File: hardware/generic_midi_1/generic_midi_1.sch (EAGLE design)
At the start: 26 parts, among them IC1 MEGA168/328, IC2 RFM12

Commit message: test
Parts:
- removed JP10: PD6, pinhead:PINHD-1X1
- removed JP11: PD4, pinhead:PINHD-1X1
- removed JP12: PD3, pinhead:PINHD-1X1
- removed JP13: PB7, pinhead:PINHD-1X1
- removed JP14: PD0, pinhead:PINHD-1X1
- removed JP9: PD5, pinhead:PINHD-1X1
- JP6: value PB1 -> (none); device pinhead:PINHD-1X1 -> pinhead:PINHD-1X8
- JP7: value PB2 -> (none); device pinhead:PINHD-1X1 -> pinhead:PINHD-1X2
- JP8: value PD1 -> (none)
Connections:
- removed net N$16: IC1.PD6(AIN0/OC0A/PCINT22), JP10.1
- removed net N$17: IC1.PB1(OC1A/PCINT1), JP6.1
- removed net N$19: IC1.PB2(SS/OC1B/PCINT2), JP7.1
- removed net N$20: IC1.PD1(TXD/PCINT17), JP8.1
- removed net N$22: IC1.PD4(T0/XCK/PCINT20), JP11.1
- removed net N$23: IC1.PD3(INT1/OC2B/PCINT19), JP12.1
- removed net N$25: IC1.PB7(XTAL2/TOSC2/PCINT7), JP13.1
- removed net N$26: IC1.PD0(RXD/PCINT16), JP14.1
- new net IO0: IC1.PD1(TXD/PCINT17), JP6.1
- new net IO1: IC1.PD0(RXD/PCINT16), JP6.2
- new net IO2: IC1.PD3(INT1/OC2B/PCINT19), JP6.3
- new net IO3: IC1.PD4(T0/XCK/PCINT20), JP6.4
- new net IO4: IC1.PD5(T1/OC0B/PCINT21), JP6.5
- new net IO5: IC1.PD6(AIN0/OC0A/PCINT22), JP6.6
- new net IO6: IC1.PB1(OC1A/PCINT1), JP6.7
- new net IO7: IC1.PB2(SS/OC1B/PCINT2), JP6.8
- net N$14: now also IC1.PB7(XTAL2/TOSC2/PCINT7), JP7.1, JP7.2; no longer IC1.PD5(T1/OC0B/PCINT21), JP9.1
- net N$24: now also JP8.1
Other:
- moved on the sheet: JP8, R2, R3

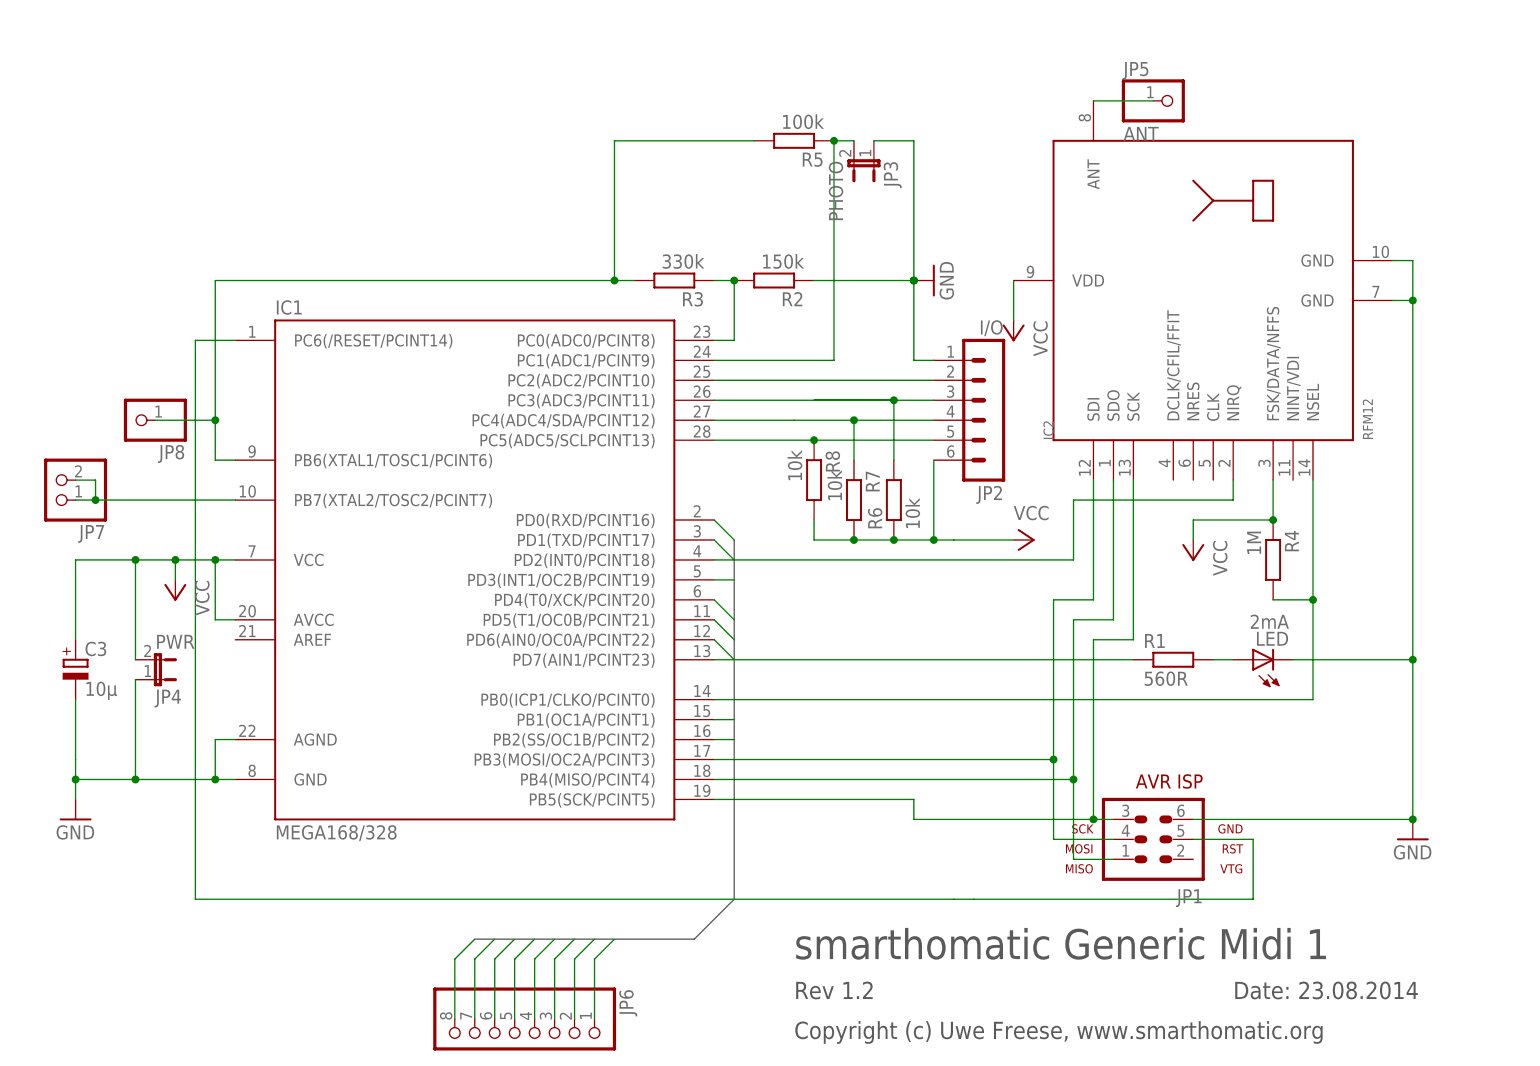
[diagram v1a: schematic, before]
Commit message: fix transistor
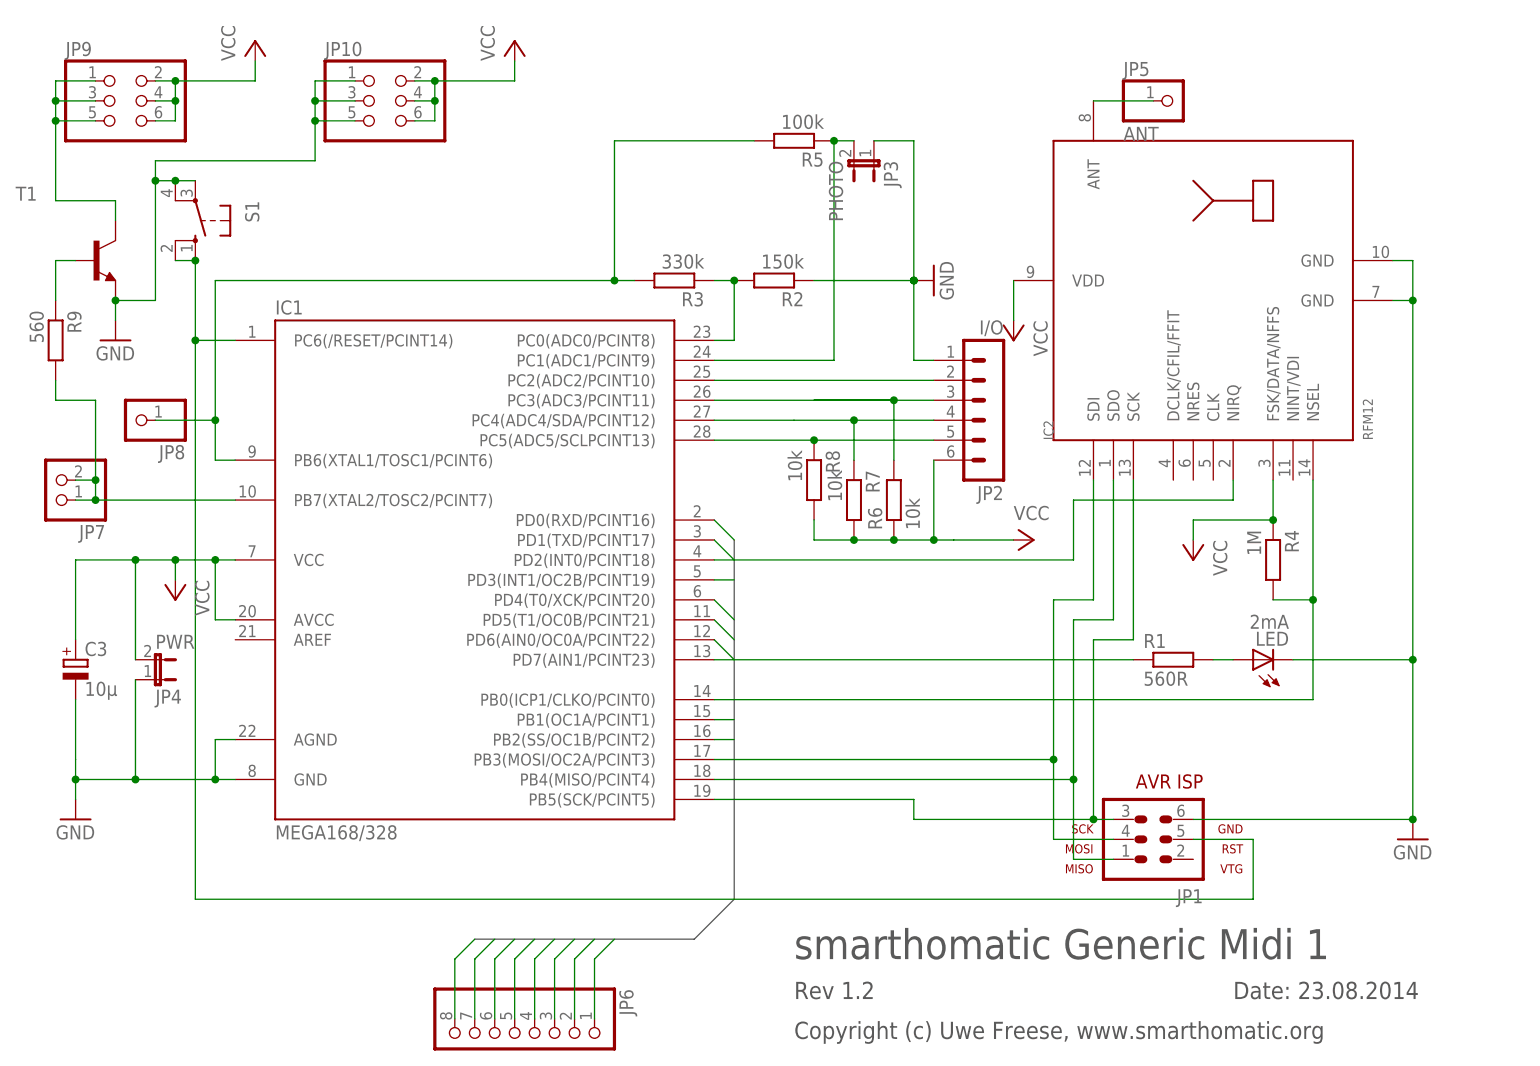
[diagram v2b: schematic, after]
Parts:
- added JP10, JP9: (no value), pinhead:PINHD-2X3
- added R9: 560, rcl:R-EU_0207/7
- added S1: (no value), switch-omron:10-XX
- added T1: (no value), transistor:BC547-NPN-TO92-CBE
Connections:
- new net N$16: JP9.1, JP9.3, JP9.5, T1.C
- new net N$17: R9.1, T1.B
- net GND: now also JP10.1, JP10.3, JP10.5, S1.P, S1.P1, T1.E
- net N$14: now also R9.2
- net N$8: now also S1.S, S1.S1
- net VCC: now also JP10.2, JP10.4, JP10.6, JP9.2, JP9.4, JP9.6
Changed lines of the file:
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@@
 <part name="JP7" library="pinhead" deviceset="PINHD-1X2" device=""/>
 <part name="JP8" library="pinhead" deviceset="PINHD-1X1" device=""/>
+<part name="JP9" library="pinhead" deviceset="PINHD-2X3" device=""/>
+<part name="JP10" library="pinhead" deviceset="PINHD-2X3" device=""/>
+<part name="T1" library="transistor" deviceset="*-NPN-" device="TO92-CBE" technology="BC547"/>
+<part name="GND4" library="supply1" deviceset="GND" device=""/>
+<part name="P+5" library="supply1" deviceset="VCC" device=""/>
+<part name="P+6" library="supply1" deviceset="VCC" device=""/>
+<part name="R9" library="rcl" deviceset="R-EU_" device="0207/7" value="560"/>
+<part name="S1" library="switch-omron" deviceset="10-XX" device=""/>
 </parts>
 <sheets>
@@
 <instance part="JP7" gate="G$1" x="-53.34" y="27.94" rot="R180"/>
 <instance part="JP8" gate="G$1" x="-43.18" y="35.56" rot="R180"/>
+<instance part="JP9" gate="A" x="-45.72" y="76.2"/>
+<instance part="JP10" gate="A" x="-12.7" y="76.2"/>
+<instance part="T1" gate="G$1" x="-48.26" y="55.88"/>
+<instance part="GND4" gate="1" x="-45.72" y="45.72"/>
+<instance part="P+5" gate="VCC" x="-27.94" y="83.82"/>
+<instance part="P+6" gate="VCC" x="5.08" y="83.82"/>
+<instance part="R9" gate="G$1" x="-53.34" y="45.72" rot="R270"/>
+<instance part="S1" gate="1" x="-35.56" y="60.96" rot="R180"/>
 </instances>
 <busses>
@@
 <junction x="55.88" y="53.34"/>
 </segment>
+<segment>
+<pinref part="T1" gate="G$1" pin="E"/>
+<pinref part="GND4" gate="1" pin="GND"/>
+<wire x1="-45.72" y1="50.8" x2="-45.72" y2="48.26" width="0.1524" layer="91"/>
+<wire x1="-45.72" y1="50.8" x2="-40.64" y2="50.8" width="0.1524" layer="91"/>
+<wire x1="-40.64" y1="50.8" x2="-40.64" y2="66.04" width="0.1524" layer="91"/>
+<junction x="-45.72" y="50.8"/>
+<wire x1="-40.64" y1="66.04" x2="-40.64" y2="68.58" width="0.1524" layer="91"/>
+<wire x1="-40.64" y1="68.58" x2="-20.32" y2="68.58" width="0.1524" layer="91"/>
+<wire x1="-20.32" y1="68.58" x2="-20.32" y2="73.66" width="0.1524" layer="91"/>
+<pinref part="JP10" gate="A" pin="5"/>
+<wire x1="-20.32" y1="73.66" x2="-15.24" y2="73.66" width="0.1524" layer="91"/>
+<pinref part="JP10" gate="A" pin="3"/>
+<wire x1="-15.24" y1="76.2" x2="-20.32" y2="76.2" width="0.1524" layer="91"/>
+<wire x1="-20.32" y1="76.2" x2="-20.32" y2="73.66" width="0.1524" layer="91"/>
+<junction x="-20.32" y="73.66"/>
+<pinref part="JP10" gate="A" pin="1"/>
+<wire x1="-15.24" y1="78.74" x2="-20.32" y2="78.74" width="0.1524" layer="91"/>
+<wire x1="-20.32" y1="78.74" x2="-20.32" y2="76.2" width="0.1524" layer="91"/>
+<junction x="-20.32" y="76.2"/>
+<pinref part="S1" gate="1" pin="P1"/>
+<pinref part="S1" gate="1" pin="P"/>
+<wire x1="-38.1" y1="66.04" x2="-35.56" y2="66.04" width="0.1524" layer="91"/>
+<wire x1="-38.1" y1="66.04" x2="-40.64" y2="66.04" width="0.1524" layer="91"/>
+<junction x="-38.1" y="66.04"/>
+<junction x="-40.64" y="66.04"/>
+</segment>
 </net>
 <net name="VCC" class="0">
@@
 <pinref part="JP2" gate="1" pin="6"/>
 </segment>
+<segment>
+<pinref part="JP9" gate="A" pin="2"/>
+<pinref part="P+5" gate="VCC" pin="VCC"/>
+<wire x1="-40.64" y1="78.74" x2="-38.1" y2="78.74" width="0.1524" layer="91"/>
+<wire x1="-38.1" y1="78.74" x2="-27.94" y2="78.74" width="0.1524" layer="91"/>
+<wire x1="-27.94" y1="78.74" x2="-27.94" y2="81.28" width="0.1524" layer="91"/>
+<pinref part="JP9" gate="A" pin="4"/>
+<wire x1="-40.64" y1="76.2" x2="-38.1" y2="76.2" width="0.1524" layer="91"/>
+<wire x1="-38.1" y1="76.2" x2="-38.1" y2="78.74" width="0.1524" layer="91"/>
+<junction x="-38.1" y="78.74"/>
+<pinref part="JP9" gate="A" pin="6"/>
+<wire x1="-40.64" y1="73.66" x2="-38.1" y2="73.66" width="0.1524" layer="91"/>
+<wire x1="-38.1" y1="73.66" x2="-38.1" y2="76.2" width="0.1524" layer="91"/>
+<junction x="-38.1" y="76.2"/>
+</segment>
+<segment>
+<pinref part="JP10" gate="A" pin="2"/>
+<pinref part="P+6" gate="VCC" pin="VCC"/>
+<wire x1="-7.62" y1="78.74" x2="-5.08" y2="78.74" width="0.1524" layer="91"/>
+<wire x1="-5.08" y1="78.74" x2="5.08" y2="78.74" width="0.1524" layer="91"/>
+<wire x1="5.08" y1="78.74" x2="5.08" y2="81.28" width="0.1524" layer="91"/>
+<pinref part="JP10" gate="A" pin="4"/>
+<wire x1="-7.62" y1="76.2" x2="-5.08" y2="76.2" width="0.1524" layer="91"/>
+<wire x1="-5.08" y1="76.2" x2="-5.08" y2="78.74" width="0.1524" layer="91"/>
+<junction x="-5.08" y="78.74"/>
+<pinref part="JP10" gate="A" pin="6"/>
+<wire x1="-7.62" y1="73.66" x2="-5.08" y2="73.66" width="0.1524" layer="91"/>
+<wire x1="-5.08" y1="73.66" x2="-5.08" y2="76.2" width="0.1524" layer="91"/>
+<junction x="-5.08" y="76.2"/>
+</segment>
 </net>
 <net name="N$3" class="0">
@@
 <wire x1="91.44" y1="-17.78" x2="99.06" y2="-17.78" width="0.1524" layer="91"/>
 <wire x1="99.06" y1="-17.78" x2="99.06" y2="-25.4" width="0.1524" layer="91"/>
-<wire x1="99.06" y1="-25.4" x2="63.5" y2="-25.4" width="0.1524" layer="91"/>
-<wire x1="63.5" y1="-25.4" x2="60.96" y2="-25.4" width="0.1524" layer="91"/>
-<wire x1="60.96" y1="-25.4" x2="-35.56" y2="-25.4" width="0.1524" layer="91"/>
+<wire x1="99.06" y1="-25.4" x2="-35.56" y2="-25.4" width="0.1524" layer="91"/>
 <pinref part="IC1" gate="1" pin="PC6(/RESET/PCINT14)"/>
 <wire x1="-35.56" y1="-25.4" x2="-35.56" y2="45.72" width="0.1524" layer="91"/>
 <wire x1="-35.56" y1="45.72" x2="-30.48" y2="45.72" width="0.1524" layer="91"/>
+<pinref part="S1" gate="1" pin="S"/>
+<wire x1="-35.56" y1="45.72" x2="-35.56" y2="55.88" width="0.1524" layer="91"/>
+<junction x="-35.56" y="45.72"/>
+<pinref part="S1" gate="1" pin="S1"/>
+<wire x1="-38.1" y1="55.88" x2="-35.56" y2="55.88" width="0.1524" layer="91"/>
+<junction x="-35.56" y="55.88"/>
 </segment>
 </net>
@@
 <wire x1="-48.26" y1="27.94" x2="-48.26" y2="25.4" width="0.1524" layer="91"/>
 <junction x="-48.26" y="25.4"/>
-</segment>
-</net>
+<wire x1="-48.26" y1="27.94" x2="-48.26" y2="38.1" width="0.1524" layer="91"/>
+<junction x="-48.26" y="27.94"/>
+<wire x1="-48.26" y1="38.1" x2="-53.34" y2="38.1" width="0.1524" layer="91"/>
+<pinref part="R9" gate="G$1" pin="2"/>
+<wire x1="-53.34" y1="38.1" x2="-53.34" y2="40.64" width="0.1524" layer="91"/>
+</segment>
+</net>
+<net name="N$16" class="0">
+<segment>
+<pinref part="T1" gate="G$1" pin="C"/>
+<wire x1="-45.72" y1="60.96" x2="-45.72" y2="63.5" width="0.1524" layer="91"/>
+<wire x1="-45.72" y1="63.5" x2="-53.34" y2="63.5" width="0.1524" layer="91"/>
+<wire x1="-53.34" y1="63.5" x2="-53.34" y2="73.66" width="0.1524" layer="91"/>
+<pinref part="JP9" gate="A" pin="5"/>
+<wire x1="-53.34" y1="73.66" x2="-48.26" y2="73.66" width="0.1524" layer="91"/>
+<wire x1="-53.34" y1="73.66" x2="-53.34" y2="76.2" width="0.1524" layer="91"/>
+<junction x="-53.34" y="73.66"/>
+<pinref part="JP9" gate="A" pin="3"/>
+<wire x1="-53.34" y1="76.2" x2="-48.26" y2="76.2" width="0.1524" layer="91"/>
+<pinref part="JP9" gate="A" pin="1"/>
+<wire x1="-48.26" y1="78.74" x2="-53.34" y2="78.74" width="0.1524" layer="91"/>
+<wire x1="-53.34" y1="78.74" x2="-53.34" y2="76.2" width="0.1524" layer="91"/>
+<junction x="-53.34" y="76.2"/>
+</segment>
+</net>
+<net name="N$17" class="0">
+<segment>
+<pinref part="T1" gate="G$1" pin="B"/>
+<wire x1="-53.34" y1="55.88" x2="-50.8" y2="55.88" width="0.1524" layer="91"/>
+<pinref part="R9" gate="G$1" pin="1"/>
+<wire x1="-53.34" y1="50.8" x2="-53.34" y2="55.88" width="0.1524" layer="91"/>
+</segment>
+</net>
